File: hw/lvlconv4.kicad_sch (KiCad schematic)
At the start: 12 parts, among them Q1 BSS138, Q2 BSS138, Q3 BSS138, Q4 BSS138

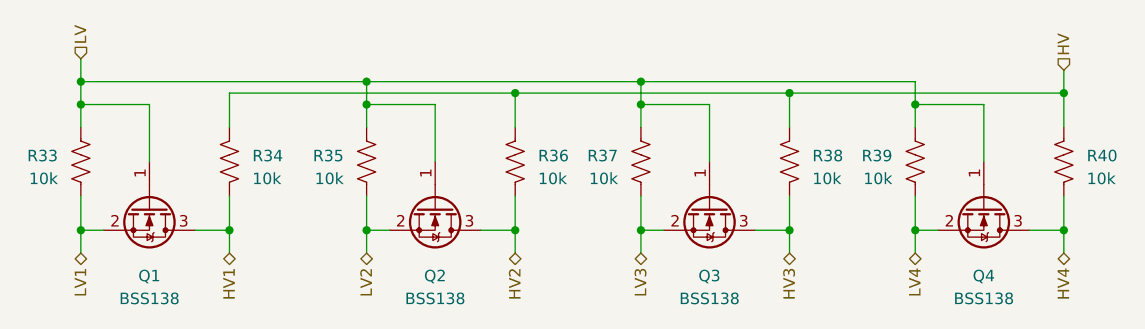
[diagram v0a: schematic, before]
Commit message: add hw schematics for video output with veraduino
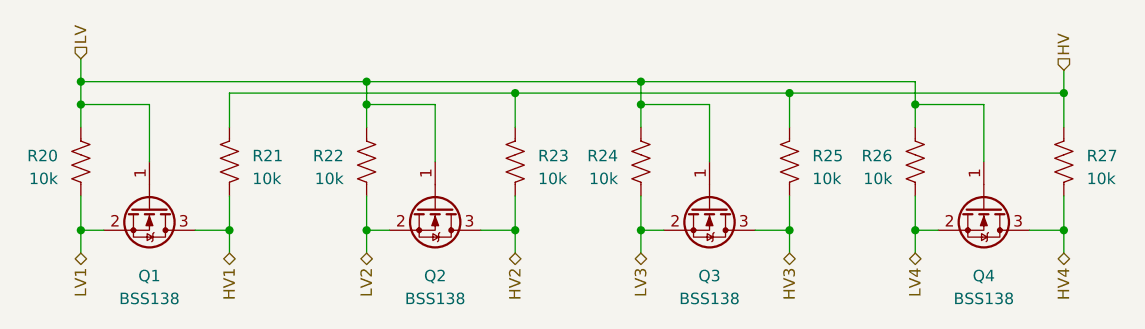
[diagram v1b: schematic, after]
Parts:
- renumbered R33 to R20, R34 to R21, R35 to R22, R36 to R23, R37 to R24, R38 to R25, R39 to R26, R40 to R27
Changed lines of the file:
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@@
   (symbol (lib_id "Device:R_US") (at 104.14 34.29 0) (mirror y) (unit 1)
     (in_bom yes) (on_board yes) (dnp no)
-    (property "Reference" "R38" (at 106.68 33.655 0)
+    (property "Reference" "R25" (at 106.68 33.655 0)
       (effects (font (size 1.27 1.27)) (justify right))
     )
@@
       (project "rod6502"
         (path "/031ea57b-8d17-4b45-87cc-c58302485ce1/483a966f-eee8-4f33-a7bb-d1365211428b/0399b11a-1c30-4b2f-a517-0d2075a1b58d"
-          (reference "R38") (unit 1)
+          (reference "R25") (unit 1)
         )
       )
@@
   (symbol (lib_id "Device:R_US") (at 87.63 34.29 0) (unit 1)
     (in_bom yes) (on_board yes) (dnp no)
-    (property "Reference" "R37" (at 85.09 33.655 0)
+    (property "Reference" "R24" (at 85.09 33.655 0)
       (effects (font (size 1.27 1.27)) (justify right))
     )
@@
       (project "rod6502"
         (path "/031ea57b-8d17-4b45-87cc-c58302485ce1/483a966f-eee8-4f33-a7bb-d1365211428b/0399b11a-1c30-4b2f-a517-0d2075a1b58d"
-          (reference "R37") (unit 1)
+          (reference "R24") (unit 1)
         )
       )
@@
   (symbol (lib_id "Device:R_US") (at 118.11 34.29 0) (unit 1)
     (in_bom yes) (on_board yes) (dnp no)
-    (property "Reference" "R39" (at 115.57 33.655 0)
+    (property "Reference" "R26" (at 115.57 33.655 0)
       (effects (font (size 1.27 1.27)) (justify right))
     )
@@
       (project "rod6502"
         (path "/031ea57b-8d17-4b45-87cc-c58302485ce1/483a966f-eee8-4f33-a7bb-d1365211428b/0399b11a-1c30-4b2f-a517-0d2075a1b58d"
-          (reference "R39") (unit 1)
+          (reference "R26") (unit 1)
         )
       )
@@
   (symbol (lib_id "Device:R_US") (at 25.4 34.29 0) (unit 1)
     (in_bom yes) (on_board yes) (dnp no)
-    (property "Reference" "R33" (at 22.86 33.655 0)
+    (property "Reference" "R20" (at 22.86 33.655 0)
       (effects (font (size 1.27 1.27)) (justify right))
     )
@@
       (project "rod6502"
         (path "/031ea57b-8d17-4b45-87cc-c58302485ce1/483a966f-eee8-4f33-a7bb-d1365211428b/0399b11a-1c30-4b2f-a517-0d2075a1b58d"
-          (reference "R33") (unit 1)
+          (reference "R20") (unit 1)
         )
       )
@@
   (symbol (lib_id "Device:R_US") (at 134.62 34.29 0) (mirror y) (unit 1)
     (in_bom yes) (on_board yes) (dnp no)
-    (property "Reference" "R40" (at 137.16 33.655 0)
+    (property "Reference" "R27" (at 137.16 33.655 0)
       (effects (font (size 1.27 1.27)) (justify right))
     )
@@
       (project "rod6502"
         (path "/031ea57b-8d17-4b45-87cc-c58302485ce1/483a966f-eee8-4f33-a7bb-d1365211428b/0399b11a-1c30-4b2f-a517-0d2075a1b58d"
-          (reference "R40") (unit 1)
+          (reference "R27") (unit 1)
         )
       )
@@
   (symbol (lib_id "Device:R_US") (at 73.66 34.29 0) (mirror y) (unit 1)
     (in_bom yes) (on_board yes) (dnp no)
-    (property "Reference" "R36" (at 76.2 33.655 0)
+    (property "Reference" "R23" (at 76.2 33.655 0)
       (effects (font (size 1.27 1.27)) (justify right))
     )
@@
       (project "rod6502"
         (path "/031ea57b-8d17-4b45-87cc-c58302485ce1/483a966f-eee8-4f33-a7bb-d1365211428b/0399b11a-1c30-4b2f-a517-0d2075a1b58d"
-          (reference "R36") (unit 1)
+          (reference "R23") (unit 1)
         )
       )
@@
   (symbol (lib_id "Device:R_US") (at 41.91 34.29 0) (mirror y) (unit 1)
     (in_bom yes) (on_board yes) (dnp no)
-    (property "Reference" "R34" (at 44.45 33.655 0)
+    (property "Reference" "R21" (at 44.45 33.655 0)
       (effects (font (size 1.27 1.27)) (justify right))
     )
@@
       (project "rod6502"
         (path "/031ea57b-8d17-4b45-87cc-c58302485ce1/483a966f-eee8-4f33-a7bb-d1365211428b/0399b11a-1c30-4b2f-a517-0d2075a1b58d"
-          (reference "R34") (unit 1)
+          (reference "R21") (unit 1)
         )
       )
@@
   (symbol (lib_id "Device:R_US") (at 57.15 34.29 0) (unit 1)
     (in_bom yes) (on_board yes) (dnp no)
-    (property "Reference" "R35" (at 54.61 33.655 0)
+    (property "Reference" "R22" (at 54.61 33.655 0)
       (effects (font (size 1.27 1.27)) (justify right))
     )
@@
       (project "rod6502"
         (path "/031ea57b-8d17-4b45-87cc-c58302485ce1/483a966f-eee8-4f33-a7bb-d1365211428b/0399b11a-1c30-4b2f-a517-0d2075a1b58d"
-          (reference "R35") (unit 1)
-        )
-      )
+          (reference "R22") (unit 1)
+        )
+      )
